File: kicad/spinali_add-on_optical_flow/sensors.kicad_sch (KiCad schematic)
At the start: 38 parts, among them Q1 BC817, Q2 BC868, U1 AFBR-S50LX85D, U2 PAA3905E1, U3 ICM-45686, U4 ICM-42688-P

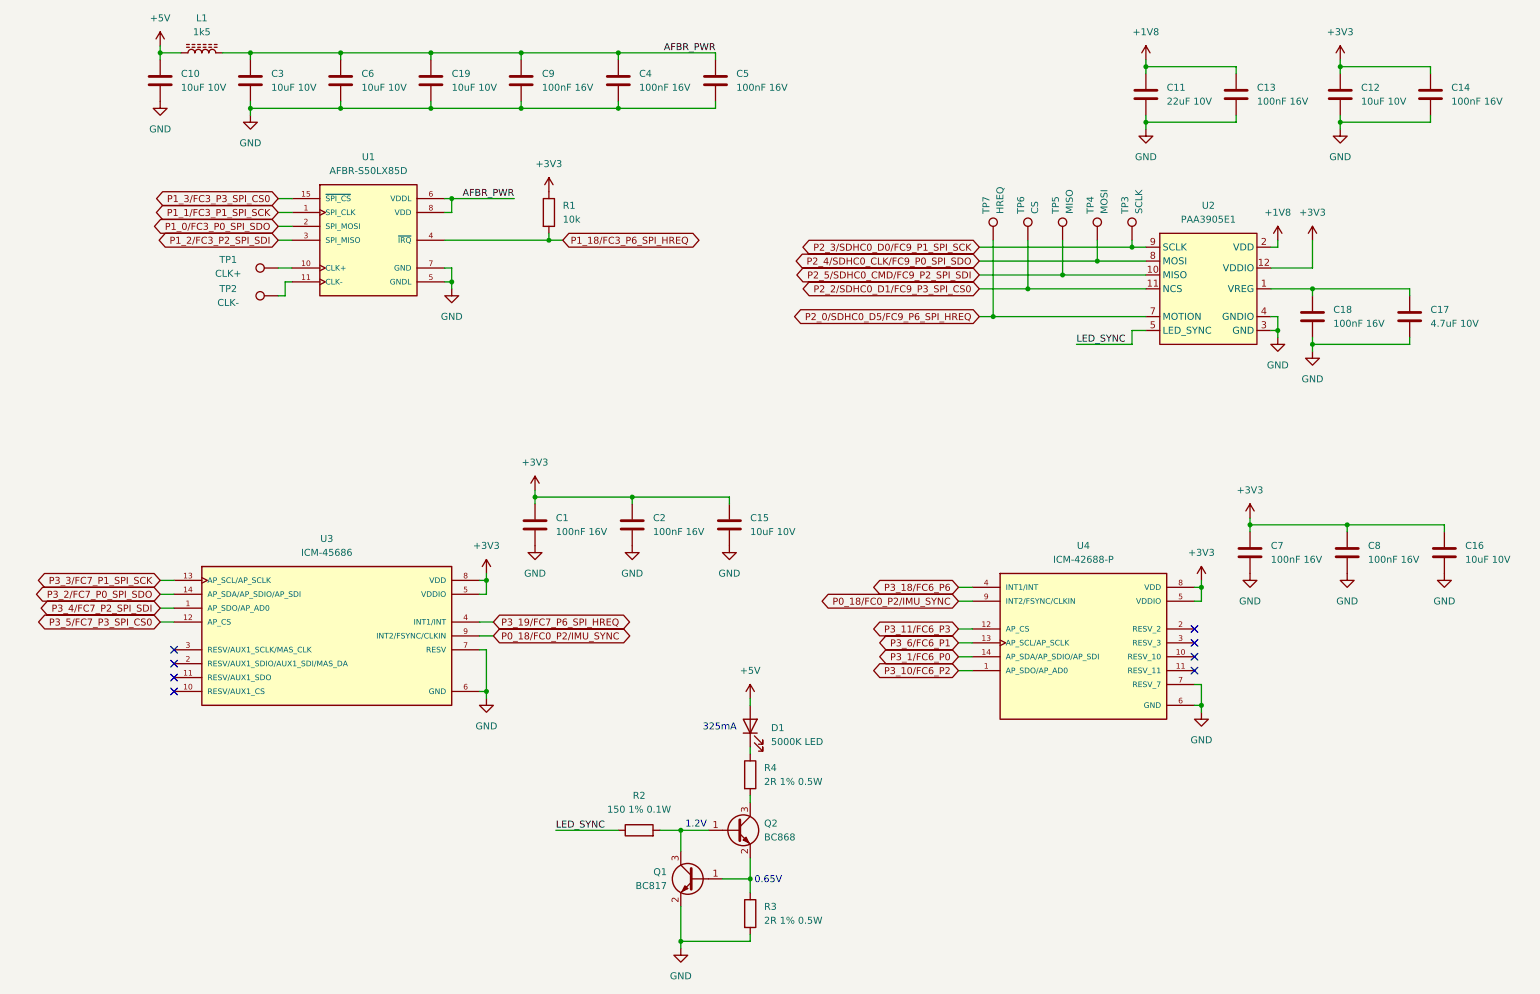
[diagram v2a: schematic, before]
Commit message: Finalized design for V0 production
- Added correct BOM and Gerbers
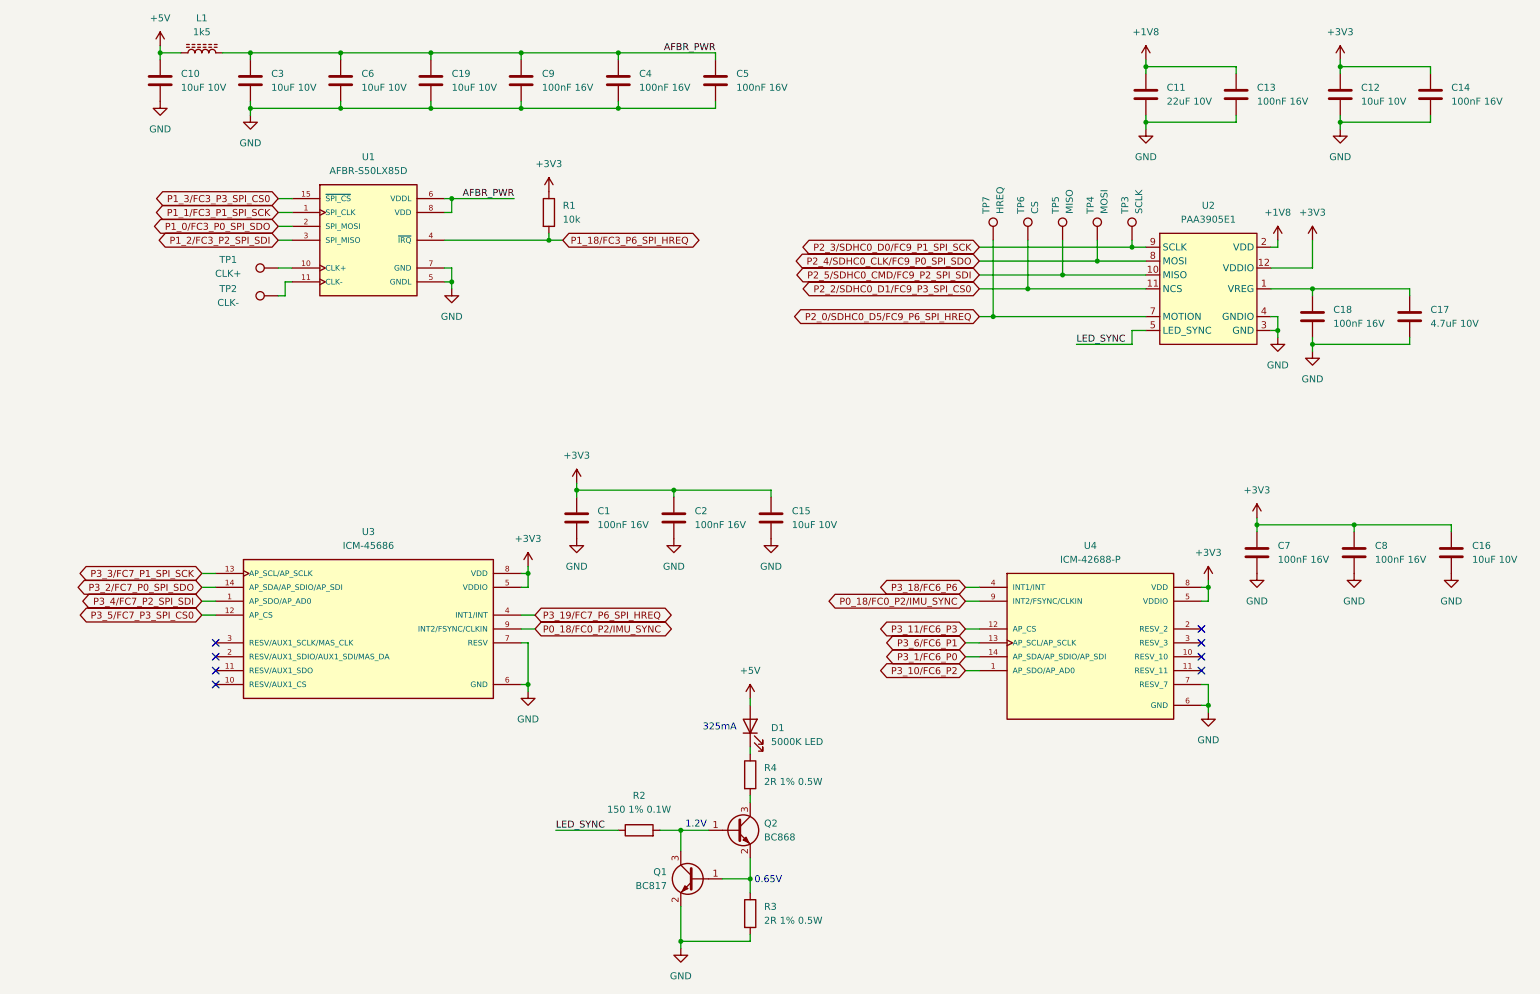
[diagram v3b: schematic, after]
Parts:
- U2: Codico (none) -> 318864; MFPN (none) -> PAA3905E1-Q
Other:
- moved on the sheet: C1, C15, C16, C2, C7, C8, U3, U4

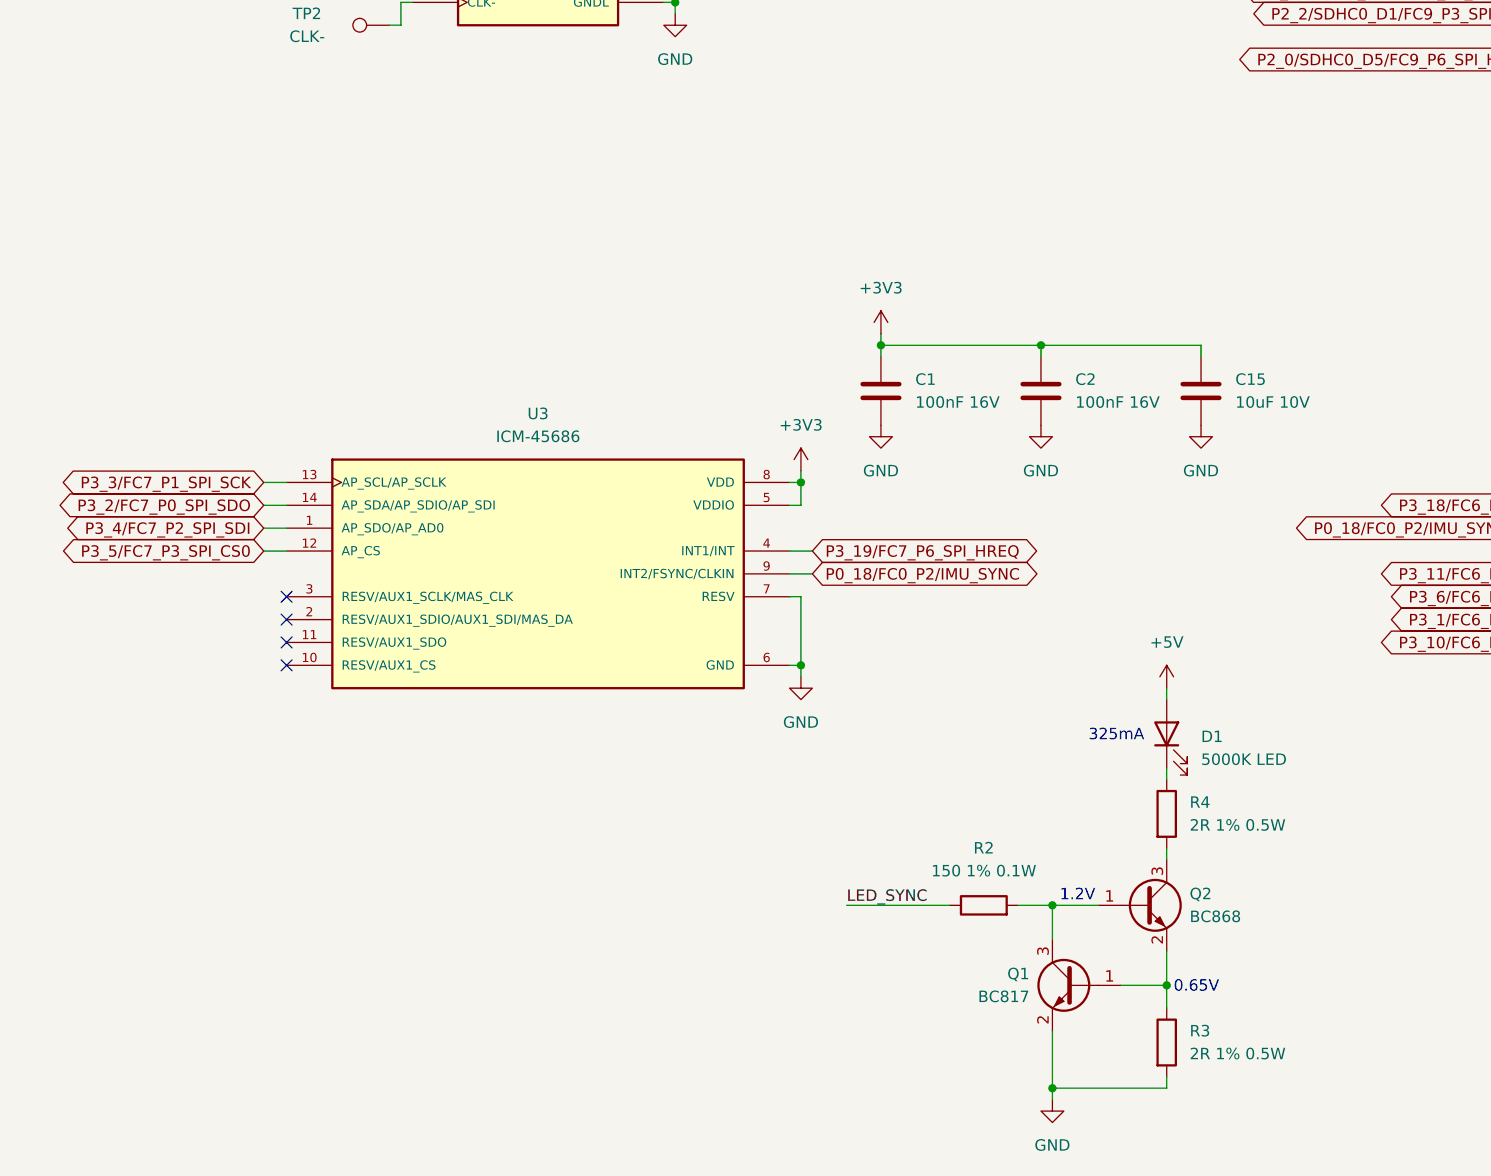
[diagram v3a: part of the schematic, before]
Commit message: Updated Optical flow add-on board
- Added patch for inverting LED_SYNC signal coming from PAA3905.
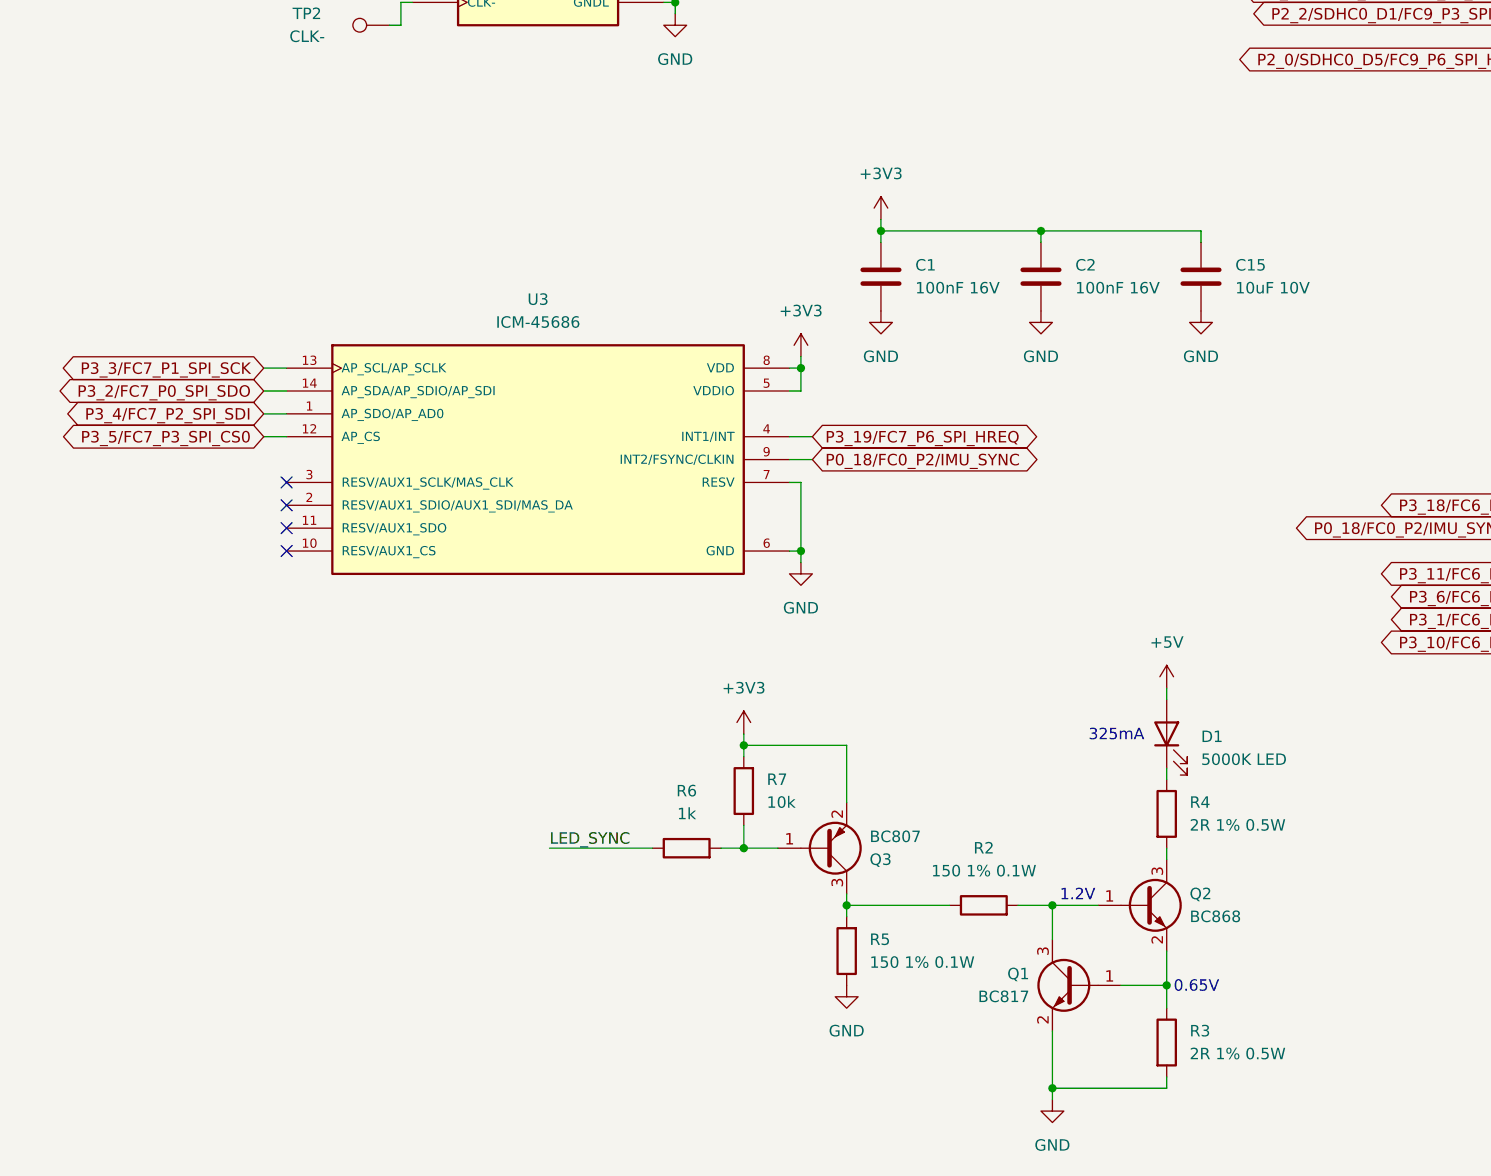
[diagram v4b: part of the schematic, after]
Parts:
- added Q3: BC807, Package_TO_SOT_SMD:SOT-23, symbol Transistor_BJT:BC807
- added R5: 150 1% 0.1W, Resistor_SMD:R_0603_1608Metric, symbol Device:R
- added R6: 1k, Resistor_SMD:R_0603_1608Metric, symbol Device:R
- added R7: 10k, Resistor_SMD:R_0603_1608Metric, symbol Device:R
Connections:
- net +3V3: now also Q3.2 (E), R7.2
- net GND: now also R5.1
- net LED_SYNC: now also R6.1; no longer R2.1
- new net: Q3.3 (C), R2.1, R5.2
- new net: Q3.1 (B), R6.2, R7.1
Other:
- moved on the sheet: C1, C15, C2, U3
